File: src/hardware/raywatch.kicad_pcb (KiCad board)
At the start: 2 copper layers, 388 parts, among them J1 Conn_01x02_Pin, J10 Conn_01x04_Pin, J11 Conn_01x04_Pin, J12 Conn_01x02_Pin, J13 Conn_01x02_Pin, J14 Conn_02x08_Top_Bottom, J15 Conn_02x08_Top_Bottom, J16 Conn_02x08_Top_Bottom, J17 Conn_02x08_Top_Bottom, J18 Conn_01x02_Pin, J19 Conn_01x02_Pin, J2 Conn_01x02_Pin, J20 Conn_01x02_Pin, J21 Conn_02x08_Top_Bottom, J22 Conn_01x02_Pin, J23 Conn_01x04_Pin, J24 Conn_01x02_Pin, J25 Conn_01x02_Pin, J26 Conn_01x02_Pin, J27 Conn_01x01_Pin, J28 Conn_01x01_Pin, J29 Conn_01x02_Pin, J3 Conn_01x02_Pin, J30 Conn_01x04_Pin, J31 Conn_01x04_Pin, J32 Conn_01x01_Pin, J33 Conn_01x01_Pin, J34 046809612110846+, J35 Conn_01x02_Pin, J36 Conn_01x02_Pin, J37 Conn_01x02_Pin, J38 Conn_01x02_Pin, J39 Conn_01x02_Pin, J4 Conn_01x02_Pin, J40 Conn_01x02_Pin, J41 Conn_01x02_Pin, J42 Conn_01x02_Pin, J43 Conn_01x02_Pin, J44 Conn_01x02_Pin, J45 Conn_01x02_Pin, J46 Conn_01x02_Pin, J47 Conn_01x02_Pin, J48 Conn_01x02_Pin, J49 Conn_01x02_Pin, J5 Conn_01x02_Pin, J50 Conn_01x04_Pin, J51 MSD-1-A, J52 Conn_01x02_Pin, J53 Conn_01x02_Pin, J54 Conn_01x01_Pin, J55 Conn_01x02_Pin, J56 Conn_01x02_Pin, J57 Conn_01x02_Pin, J58 Conn_01x02_Pin, J59 Conn_01x02_Pin, J6 Conn_01x04_Pin, J60 Conn_01x02_Pin, J61 Conn_01x02_Pin, J62 Conn_01x01_Pin, J63 Conn_01x02_Pin, J64 Conn_01x02_Pin, J65 Conn_01x04_Pin, J66 Conn_01x04_Pin, J67 Conn_01x02_Pin, J68 Conn_01x02_Pin, J69 Conn_01x02_Pin, J7 Conn_01x04_Pin, J70 Conn_02x08_Top_Bottom, J71 Conn_01x02_Pin, J72 Conn_01x01_Pin, J73 Conn_02x08_Top_Bottom, J74 Conn_01x02_Pin, J75 Conn_02x08_Top_Bottom, J76 BM29B0.6-2DS/2-0.35V51, J77 Conn_01x02_Pin, J78 Conn_01x02_Pin, J79 Conn_01x02_Pin, J8 Conn_01x04_Pin, J80 Conn_01x02_Pin, J81 Conn_01x04_Pin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

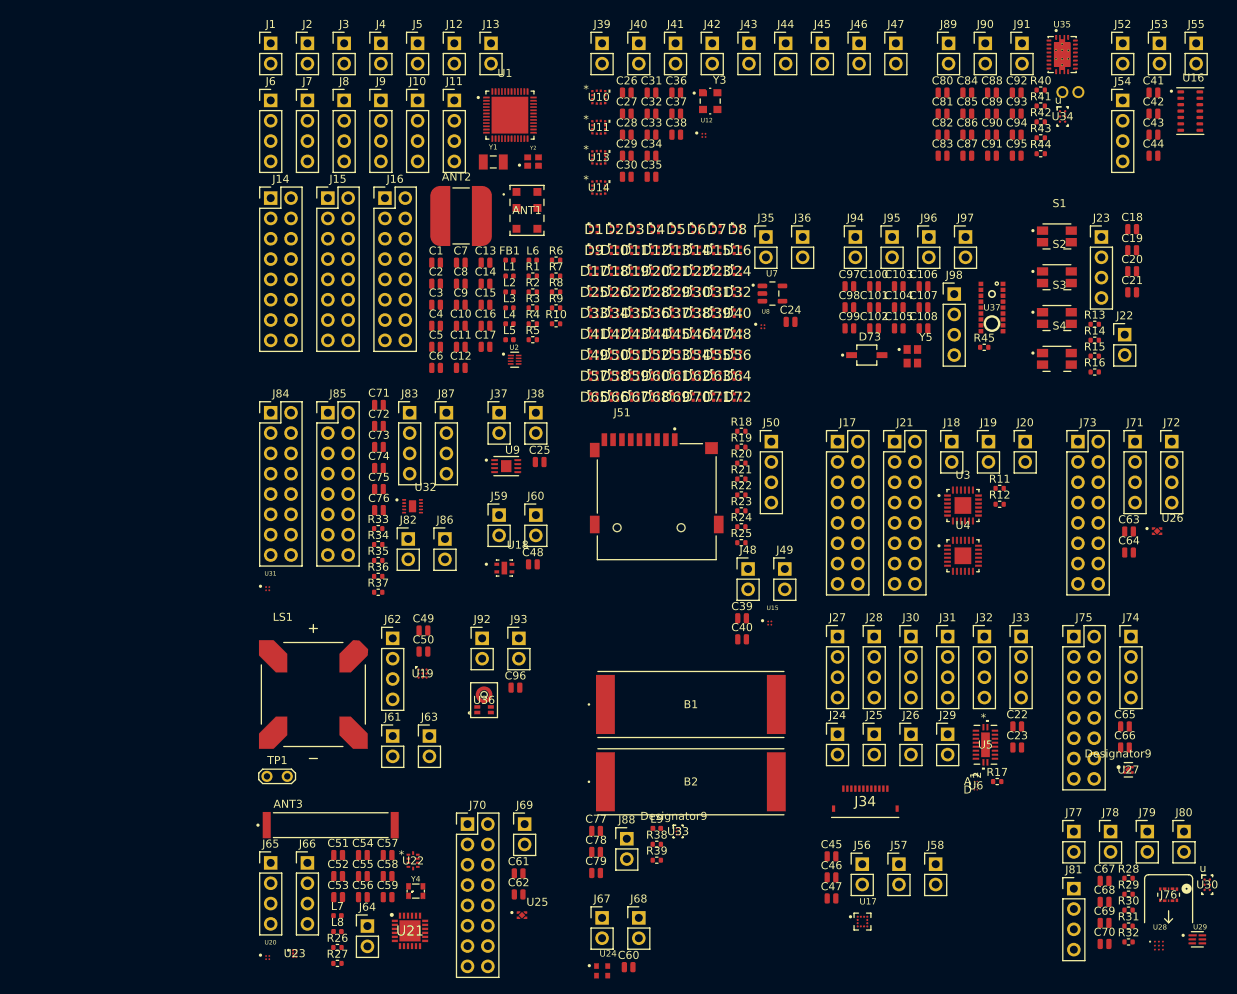
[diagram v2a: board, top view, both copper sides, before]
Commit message: Fixed connector footprints; Changed conectors from 2.54 to 1.27
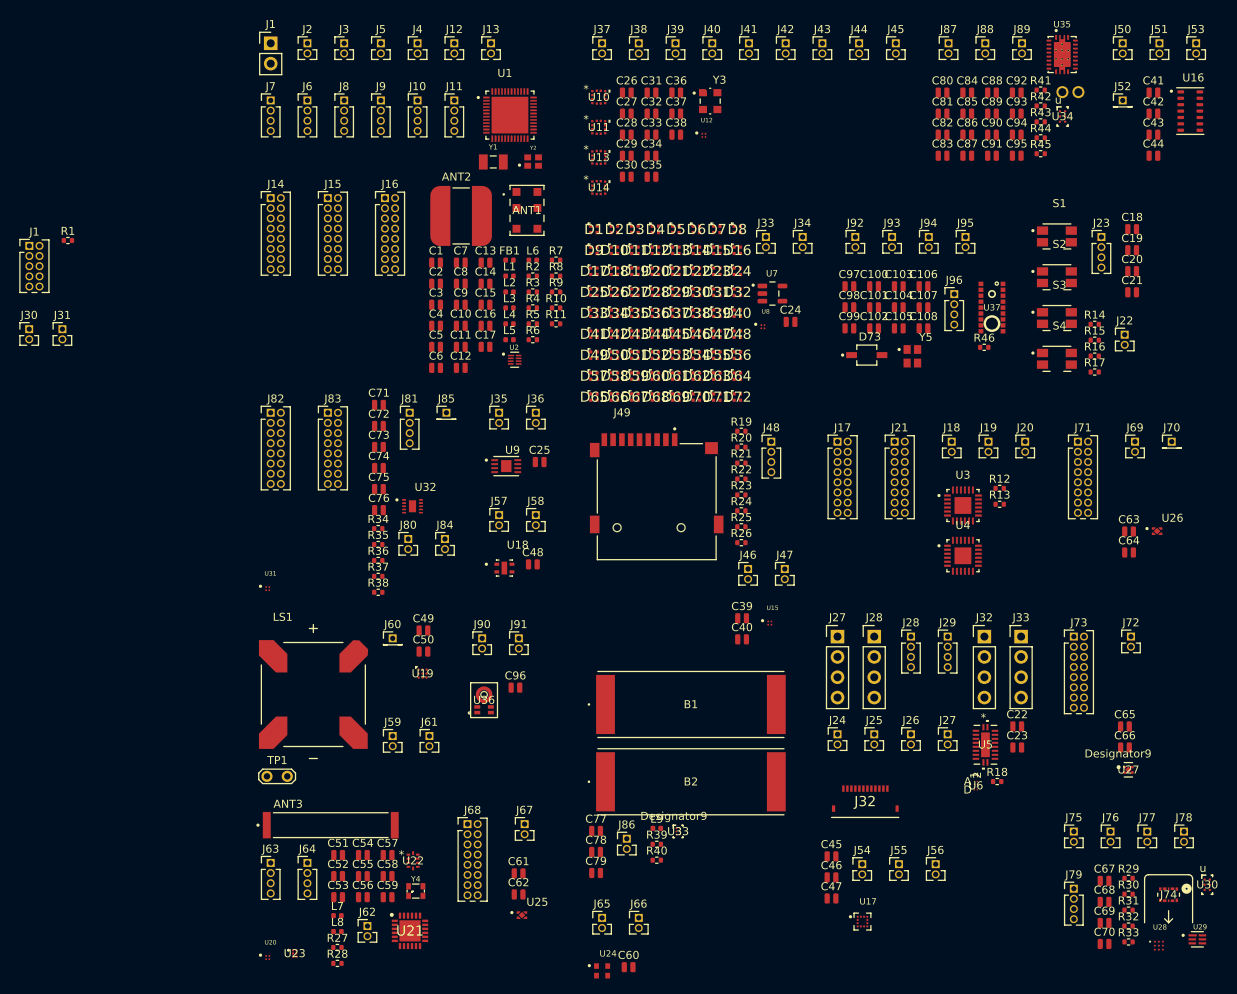
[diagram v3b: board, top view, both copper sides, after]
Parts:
- added J1: Conn_02x05_Odd_Even, Connector_PinHeader_1.27mm:PinHeader_2x05_P1.27mm_Vertical, F.Cu at (54.4, 65.3)
- added J30: Conn_01x02_Pin, Connector_PinHeader_1.27mm:PinHeader_1x02_P1.27mm_Vertical, F.Cu at (54.4, 75.7)
- added J31: Conn_01x02_Pin, Connector_PinHeader_1.27mm:PinHeader_1x02_P1.27mm_Vertical, F.Cu at (58.5, 75.7)
- added R1: 1kΩ, Resistor_SMD:R_0402_1005Metric, F.Cu at (59.2, 64.7)
- J10, J11, J23, J8, J9: footprint Connector_PinHeader_2.54mm:PinHeader_1x04_P2.54mm_Vertical -> Connector_PinHeader_1.27mm:PinHeader_1x04_P1.27mm_Vertical
- J12, J13, J18, J19, J2, J20, J22, J24, J25, J26, J3: footprint Connector_PinHeader_2.54mm:PinHeader_1x02_P2.54mm_Vertical -> Connector_PinHeader_1.27mm:PinHeader_1x02_P1.27mm_Vertical
- J14, J15, J16, J17, J21: footprint Connector_PinHeader_2.54mm:PinHeader_2x08_P2.54mm_Vertical -> Connector_PinHeader_1.27mm:PinHeader_2x08_P1.27mm_Vertical
- J27: renamed from J29; footprint Connector_PinHeader_2.54mm:PinHeader_1x02_P2.54mm_Vertical -> Connector_PinHeader_1.27mm:PinHeader_1x02_P1.27mm_Vertical
- J28: renamed from J30; footprint Connector_PinHeader_2.54mm:PinHeader_1x04_P2.54mm_Vertical -> Connector_PinHeader_1.27mm:PinHeader_1x04_P1.27mm_Vertical
- J29: renamed from J31; footprint Connector_PinHeader_2.54mm:PinHeader_1x04_P2.54mm_Vertical -> Connector_PinHeader_1.27mm:PinHeader_1x04_P1.27mm_Vertical
- J33: renamed from J35; footprint Connector_PinHeader_2.54mm:PinHeader_1x02_P2.54mm_Vertical -> Connector_PinHeader_1.27mm:PinHeader_1x02_P1.27mm_Vertical
- J34: renamed from J36; footprint Connector_PinHeader_2.54mm:PinHeader_1x02_P2.54mm_Vertical -> Connector_PinHeader_1.27mm:PinHeader_1x02_P1.27mm_Vertical
- J35: renamed from J37; footprint Connector_PinHeader_2.54mm:PinHeader_1x02_P2.54mm_Vertical -> Connector_PinHeader_1.27mm:PinHeader_1x02_P1.27mm_Vertical
- J36: renamed from J38; footprint Connector_PinHeader_2.54mm:PinHeader_1x02_P2.54mm_Vertical -> Connector_PinHeader_1.27mm:PinHeader_1x02_P1.27mm_Vertical
- J37: renamed from J39; footprint Connector_PinHeader_2.54mm:PinHeader_1x02_P2.54mm_Vertical -> Connector_PinHeader_1.27mm:PinHeader_1x02_P1.27mm_Vertical
- J38: renamed from J40; footprint Connector_PinHeader_2.54mm:PinHeader_1x02_P2.54mm_Vertical -> Connector_PinHeader_1.27mm:PinHeader_1x02_P1.27mm_Vertical
- J39: renamed from J41; footprint Connector_PinHeader_2.54mm:PinHeader_1x02_P2.54mm_Vertical -> Connector_PinHeader_1.27mm:PinHeader_1x02_P1.27mm_Vertical
- J4: renamed from J5; footprint Connector_PinHeader_2.54mm:PinHeader_1x02_P2.54mm_Vertical -> Connector_PinHeader_1.27mm:PinHeader_1x02_P1.27mm_Vertical
- J40: renamed from J42; footprint Connector_PinHeader_2.54mm:PinHeader_1x02_P2.54mm_Vertical -> Connector_PinHeader_1.27mm:PinHeader_1x02_P1.27mm_Vertical
- J41: renamed from J43; footprint Connector_PinHeader_2.54mm:PinHeader_1x02_P2.54mm_Vertical -> Connector_PinHeader_1.27mm:PinHeader_1x02_P1.27mm_Vertical
- J42: renamed from J44; footprint Connector_PinHeader_2.54mm:PinHeader_1x02_P2.54mm_Vertical -> Connector_PinHeader_1.27mm:PinHeader_1x02_P1.27mm_Vertical
- J43: renamed from J45; footprint Connector_PinHeader_2.54mm:PinHeader_1x02_P2.54mm_Vertical -> Connector_PinHeader_1.27mm:PinHeader_1x02_P1.27mm_Vertical
- J44: renamed from J46; footprint Connector_PinHeader_2.54mm:PinHeader_1x02_P2.54mm_Vertical -> Connector_PinHeader_1.27mm:PinHeader_1x02_P1.27mm_Vertical
- J45: renamed from J47; footprint Connector_PinHeader_2.54mm:PinHeader_1x02_P2.54mm_Vertical -> Connector_PinHeader_1.27mm:PinHeader_1x02_P1.27mm_Vertical
- J46: renamed from J48; footprint Connector_PinHeader_2.54mm:PinHeader_1x02_P2.54mm_Vertical -> Connector_PinHeader_1.27mm:PinHeader_1x02_P1.27mm_Vertical
- J47: renamed from J49; footprint Connector_PinHeader_2.54mm:PinHeader_1x02_P2.54mm_Vertical -> Connector_PinHeader_1.27mm:PinHeader_1x02_P1.27mm_Vertical
- J48: renamed from J50; footprint Connector_PinHeader_2.54mm:PinHeader_1x04_P2.54mm_Vertical -> Connector_PinHeader_1.27mm:PinHeader_1x04_P1.27mm_Vertical
- J5: renamed from J4; footprint Connector_PinHeader_2.54mm:PinHeader_1x02_P2.54mm_Vertical -> Connector_PinHeader_1.27mm:PinHeader_1x02_P1.27mm_Vertical
- J50: renamed from J52; footprint Connector_PinHeader_2.54mm:PinHeader_1x02_P2.54mm_Vertical -> Connector_PinHeader_1.27mm:PinHeader_1x02_P1.27mm_Vertical
- J51: renamed from J53; footprint Connector_PinHeader_2.54mm:PinHeader_1x02_P2.54mm_Vertical -> Connector_PinHeader_1.27mm:PinHeader_1x02_P1.27mm_Vertical
- J52: renamed from J54; footprint Connector_PinHeader_2.54mm:PinHeader_1x04_P2.54mm_Vertical -> Connector_PinHeader_1.27mm:PinHeader_1x01_P1.27mm_Vertical
- J53: renamed from J55; footprint Connector_PinHeader_2.54mm:PinHeader_1x02_P2.54mm_Vertical -> Connector_PinHeader_1.27mm:PinHeader_1x02_P1.27mm_Vertical
- J54: renamed from J56; footprint Connector_PinHeader_2.54mm:PinHeader_1x02_P2.54mm_Vertical -> Connector_PinHeader_1.27mm:PinHeader_1x02_P1.27mm_Vertical
- J55: renamed from J57; footprint Connector_PinHeader_2.54mm:PinHeader_1x02_P2.54mm_Vertical -> Connector_PinHeader_1.27mm:PinHeader_1x02_P1.27mm_Vertical
- J56: renamed from J58; footprint Connector_PinHeader_2.54mm:PinHeader_1x02_P2.54mm_Vertical -> Connector_PinHeader_1.27mm:PinHeader_1x02_P1.27mm_Vertical
- J57: renamed from J59; footprint Connector_PinHeader_2.54mm:PinHeader_1x02_P2.54mm_Vertical -> Connector_PinHeader_1.27mm:PinHeader_1x02_P1.27mm_Vertical
- J58: renamed from J60; footprint Connector_PinHeader_2.54mm:PinHeader_1x02_P2.54mm_Vertical -> Connector_PinHeader_1.27mm:PinHeader_1x02_P1.27mm_Vertical
- J59: renamed from J61; footprint Connector_PinHeader_2.54mm:PinHeader_1x02_P2.54mm_Vertical -> Connector_PinHeader_1.27mm:PinHeader_1x02_P1.27mm_Vertical
- J6: renamed from J7; footprint Connector_PinHeader_2.54mm:PinHeader_1x04_P2.54mm_Vertical -> Connector_PinHeader_1.27mm:PinHeader_1x04_P1.27mm_Vertical
- J60: renamed from J62; footprint Connector_PinHeader_2.54mm:PinHeader_1x04_P2.54mm_Vertical -> Connector_PinHeader_1.27mm:PinHeader_1x01_P1.27mm_Vertical
- J61: renamed from J63; footprint Connector_PinHeader_2.54mm:PinHeader_1x02_P2.54mm_Vertical -> Connector_PinHeader_1.27mm:PinHeader_1x02_P1.27mm_Vertical
- J62: renamed from J64; footprint Connector_PinHeader_2.54mm:PinHeader_1x02_P2.54mm_Vertical -> Connector_PinHeader_1.27mm:PinHeader_1x02_P1.27mm_Vertical
- J63: renamed from J65; footprint Connector_PinHeader_2.54mm:PinHeader_1x04_P2.54mm_Vertical -> Connector_PinHeader_1.27mm:PinHeader_1x04_P1.27mm_Vertical
- J64: renamed from J66; footprint Connector_PinHeader_2.54mm:PinHeader_1x04_P2.54mm_Vertical -> Connector_PinHeader_1.27mm:PinHeader_1x04_P1.27mm_Vertical
- J65: renamed from J67; footprint Connector_PinHeader_2.54mm:PinHeader_1x02_P2.54mm_Vertical -> Connector_PinHeader_1.27mm:PinHeader_1x02_P1.27mm_Vertical
- J66: renamed from J68; footprint Connector_PinHeader_2.54mm:PinHeader_1x02_P2.54mm_Vertical -> Connector_PinHeader_1.27mm:PinHeader_1x02_P1.27mm_Vertical
- J67: renamed from J69; footprint Connector_PinHeader_2.54mm:PinHeader_1x02_P2.54mm_Vertical -> Connector_PinHeader_1.27mm:PinHeader_1x02_P1.27mm_Vertical
- J68: renamed from J70; footprint Connector_PinHeader_2.54mm:PinHeader_2x08_P2.54mm_Vertical -> Connector_PinHeader_1.27mm:PinHeader_2x08_P1.27mm_Vertical
- J69: renamed from J71; footprint Connector_PinHeader_2.54mm:PinHeader_1x04_P2.54mm_Vertical -> Connector_PinHeader_1.27mm:PinHeader_1x02_P1.27mm_Vertical
- J7: renamed from J6; footprint Connector_PinHeader_2.54mm:PinHeader_1x04_P2.54mm_Vertical -> Connector_PinHeader_1.27mm:PinHeader_1x04_P1.27mm_Vertical
- J70: renamed from J72; footprint Connector_PinHeader_2.54mm:PinHeader_1x04_P2.54mm_Vertical -> Connector_PinHeader_1.27mm:PinHeader_1x01_P1.27mm_Vertical
- J71: renamed from J73; footprint Connector_PinHeader_2.54mm:PinHeader_2x08_P2.54mm_Vertical -> Connector_PinHeader_1.27mm:PinHeader_2x08_P1.27mm_Vertical
- J72: renamed from J74; footprint Connector_PinHeader_2.54mm:PinHeader_1x04_P2.54mm_Vertical -> Connector_PinHeader_1.27mm:PinHeader_1x02_P1.27mm_Vertical
- J73: renamed from J75; footprint Connector_PinHeader_2.54mm:PinHeader_2x08_P2.54mm_Vertical -> Connector_PinHeader_1.27mm:PinHeader_2x08_P1.27mm_Vertical
- J75: renamed from J77; footprint Connector_PinHeader_2.54mm:PinHeader_1x02_P2.54mm_Vertical -> Connector_PinHeader_1.27mm:PinHeader_1x02_P1.27mm_Vertical
- J76: renamed from J78; footprint Connector_PinHeader_2.54mm:PinHeader_1x02_P2.54mm_Vertical -> Connector_PinHeader_1.27mm:PinHeader_1x02_P1.27mm_Vertical
- J77: renamed from J79; footprint Connector_PinHeader_2.54mm:PinHeader_1x02_P2.54mm_Vertical -> Connector_PinHeader_1.27mm:PinHeader_1x02_P1.27mm_Vertical
- J78: renamed from J80; footprint Connector_PinHeader_2.54mm:PinHeader_1x02_P2.54mm_Vertical -> Connector_PinHeader_1.27mm:PinHeader_1x02_P1.27mm_Vertical
- J79: renamed from J81; footprint Connector_PinHeader_2.54mm:PinHeader_1x04_P2.54mm_Vertical -> Connector_PinHeader_1.27mm:PinHeader_1x04_P1.27mm_Vertical
- J80: renamed from J82; footprint Connector_PinHeader_2.54mm:PinHeader_1x02_P2.54mm_Vertical -> Connector_PinHeader_1.27mm:PinHeader_1x02_P1.27mm_Vertical
- J81: renamed from J83; footprint Connector_PinHeader_2.54mm:PinHeader_1x04_P2.54mm_Vertical -> Connector_PinHeader_1.27mm:PinHeader_1x04_P1.27mm_Vertical
- J82: renamed from J84; footprint Connector_PinHeader_2.54mm:PinHeader_2x08_P2.54mm_Vertical -> Connector_PinHeader_1.27mm:PinHeader_2x08_P1.27mm_Vertical
- J83: renamed from J85; footprint Connector_PinHeader_2.54mm:PinHeader_2x08_P2.54mm_Vertical -> Connector_PinHeader_1.27mm:PinHeader_2x08_P1.27mm_Vertical
- J84: renamed from J86; footprint Connector_PinHeader_2.54mm:PinHeader_1x02_P2.54mm_Vertical -> Connector_PinHeader_1.27mm:PinHeader_1x02_P1.27mm_Vertical
- J85: renamed from J87; footprint Connector_PinHeader_2.54mm:PinHeader_1x04_P2.54mm_Vertical -> Connector_PinHeader_1.27mm:PinHeader_1x01_P1.27mm_Vertical
- J86: renamed from J88; footprint Connector_PinHeader_2.54mm:PinHeader_1x02_P2.54mm_Vertical -> Connector_PinHeader_1.27mm:PinHeader_1x02_P1.27mm_Vertical
- J87: renamed from J89; footprint Connector_PinHeader_2.54mm:PinHeader_1x02_P2.54mm_Vertical -> Connector_PinHeader_1.27mm:PinHeader_1x02_P1.27mm_Vertical
- J88: renamed from J90; footprint Connector_PinHeader_2.54mm:PinHeader_1x02_P2.54mm_Vertical -> Connector_PinHeader_1.27mm:PinHeader_1x02_P1.27mm_Vertical
- J89: renamed from J91; footprint Connector_PinHeader_2.54mm:PinHeader_1x02_P2.54mm_Vertical -> Connector_PinHeader_1.27mm:PinHeader_1x02_P1.27mm_Vertical
- J90: renamed from J92; footprint Connector_PinHeader_2.54mm:PinHeader_1x02_P2.54mm_Vertical -> Connector_PinHeader_1.27mm:PinHeader_1x02_P1.27mm_Vertical
- J91: renamed from J93; footprint Connector_PinHeader_2.54mm:PinHeader_1x02_P2.54mm_Vertical -> Connector_PinHeader_1.27mm:PinHeader_1x02_P1.27mm_Vertical
- J92: renamed from J94; footprint Connector_PinHeader_2.54mm:PinHeader_1x02_P2.54mm_Vertical -> Connector_PinHeader_1.27mm:PinHeader_1x02_P1.27mm_Vertical
- J93: renamed from J95; footprint Connector_PinHeader_2.54mm:PinHeader_1x02_P2.54mm_Vertical -> Connector_PinHeader_1.27mm:PinHeader_1x02_P1.27mm_Vertical
- J94: renamed from J96; footprint Connector_PinHeader_2.54mm:PinHeader_1x02_P2.54mm_Vertical -> Connector_PinHeader_1.27mm:PinHeader_1x02_P1.27mm_Vertical
- J95: renamed from J97; footprint Connector_PinHeader_2.54mm:PinHeader_1x02_P2.54mm_Vertical -> Connector_PinHeader_1.27mm:PinHeader_1x02_P1.27mm_Vertical
- J96: renamed from J98; footprint Connector_PinHeader_2.54mm:PinHeader_1x04_P2.54mm_Vertical -> Connector_PinHeader_1.27mm:PinHeader_1x04_P1.27mm_Vertical
- renumbered J34 to J32, J51 to J49, J76 to J74, R9 to R10, R10 to R11, R11 to R12, R12 to R13, R13 to R14, R14 to R15, R15 to R16, R16 to R17, R17 to R18, R18 to R19, R1 to R2, R19 to R20, R20 to R21, R21 to R22, R22 to R23, R23 to R24, R24 to R25, R25 to R26, R26 to R27, R27 to R28, R28 to R29, R2 to R3, R29 to R30, R30 to R31, R31 to R32, R32 to R33, R33 to R34, R34 to R35, R35 to R36, R36 to R37, R37 to R38, R38 to R39, R3 to R4, R39 to R40, R40 to R41, R41 to R42, R42 to R43, R43 to R44, R44 to R45, R45 to R46, R4 to R5, R5 to R6, R6 to R7, R7 to R8, R8 to R9
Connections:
- net Net-(J10-Pin_2) renamed /MC: Microcontroller/P2.07
- U1 pad 26: Net-(J1-Pin_1) -> Net-(J1-Pin_4)
- U5 pad 12: Net-(J32-Pin_1) -> Net-(J30-Pin_2)
- U5 pad 13: /Display/HRINT -> Net-(J30-Pin_1)
- U5 pad 8: /Display/HRINT1V8 -> Net-(J31-Pin_1)
- U5 pad 9: Net-(J33-Pin_1) -> Net-(J31-Pin_2)

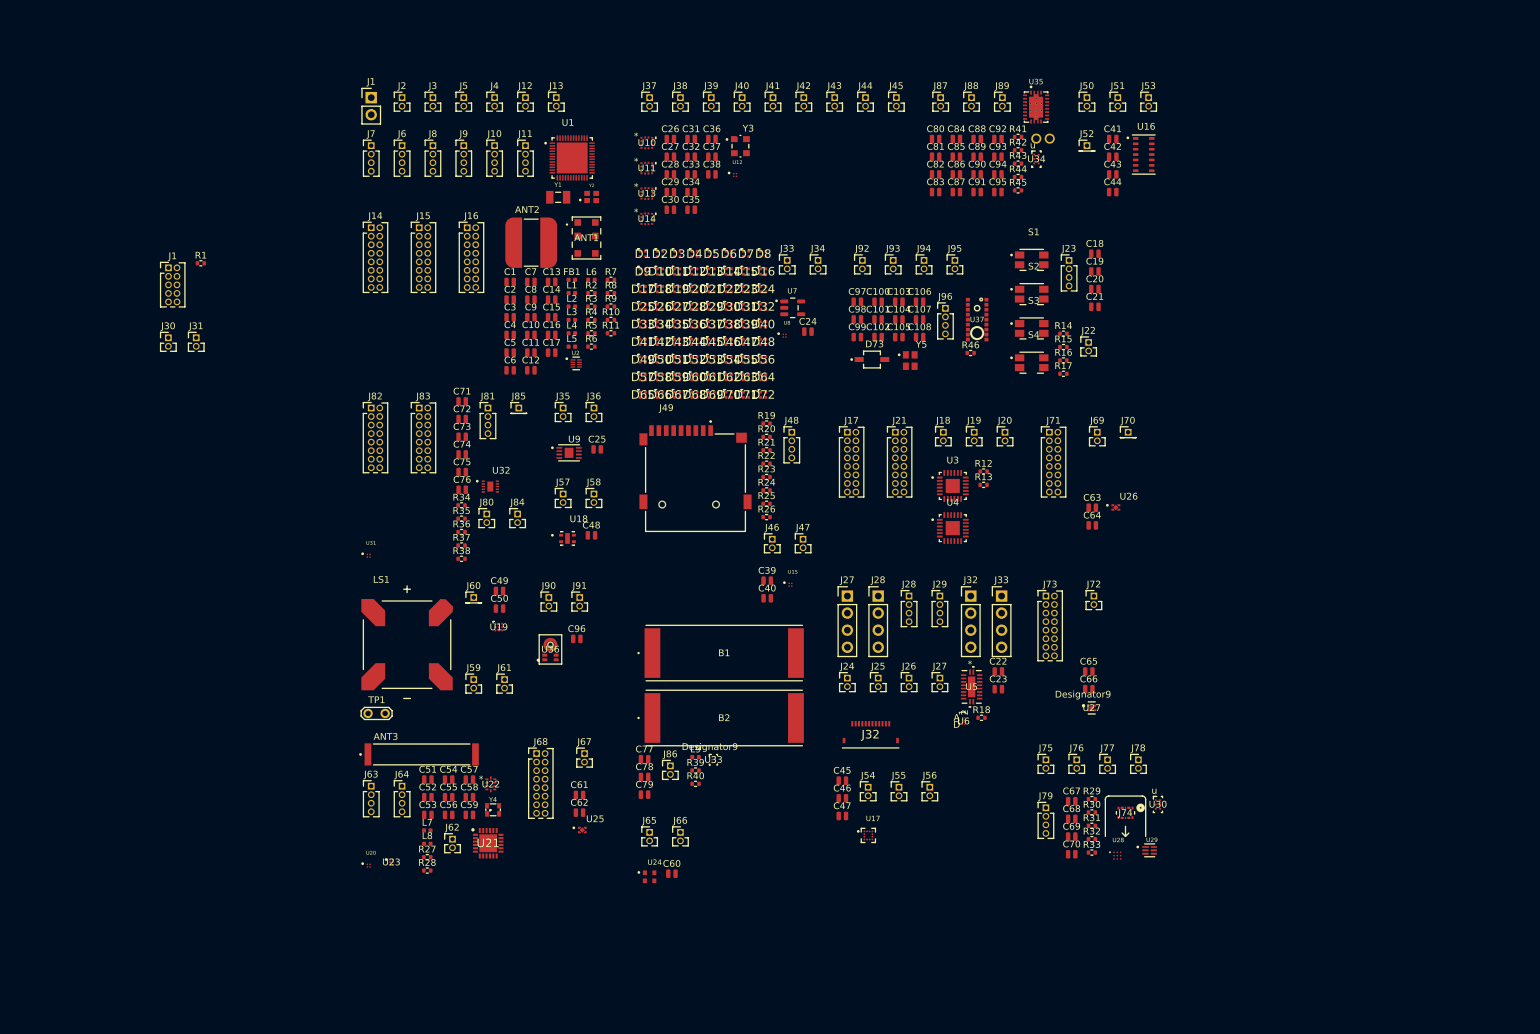
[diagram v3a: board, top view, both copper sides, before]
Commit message: Sorted footprints into modules
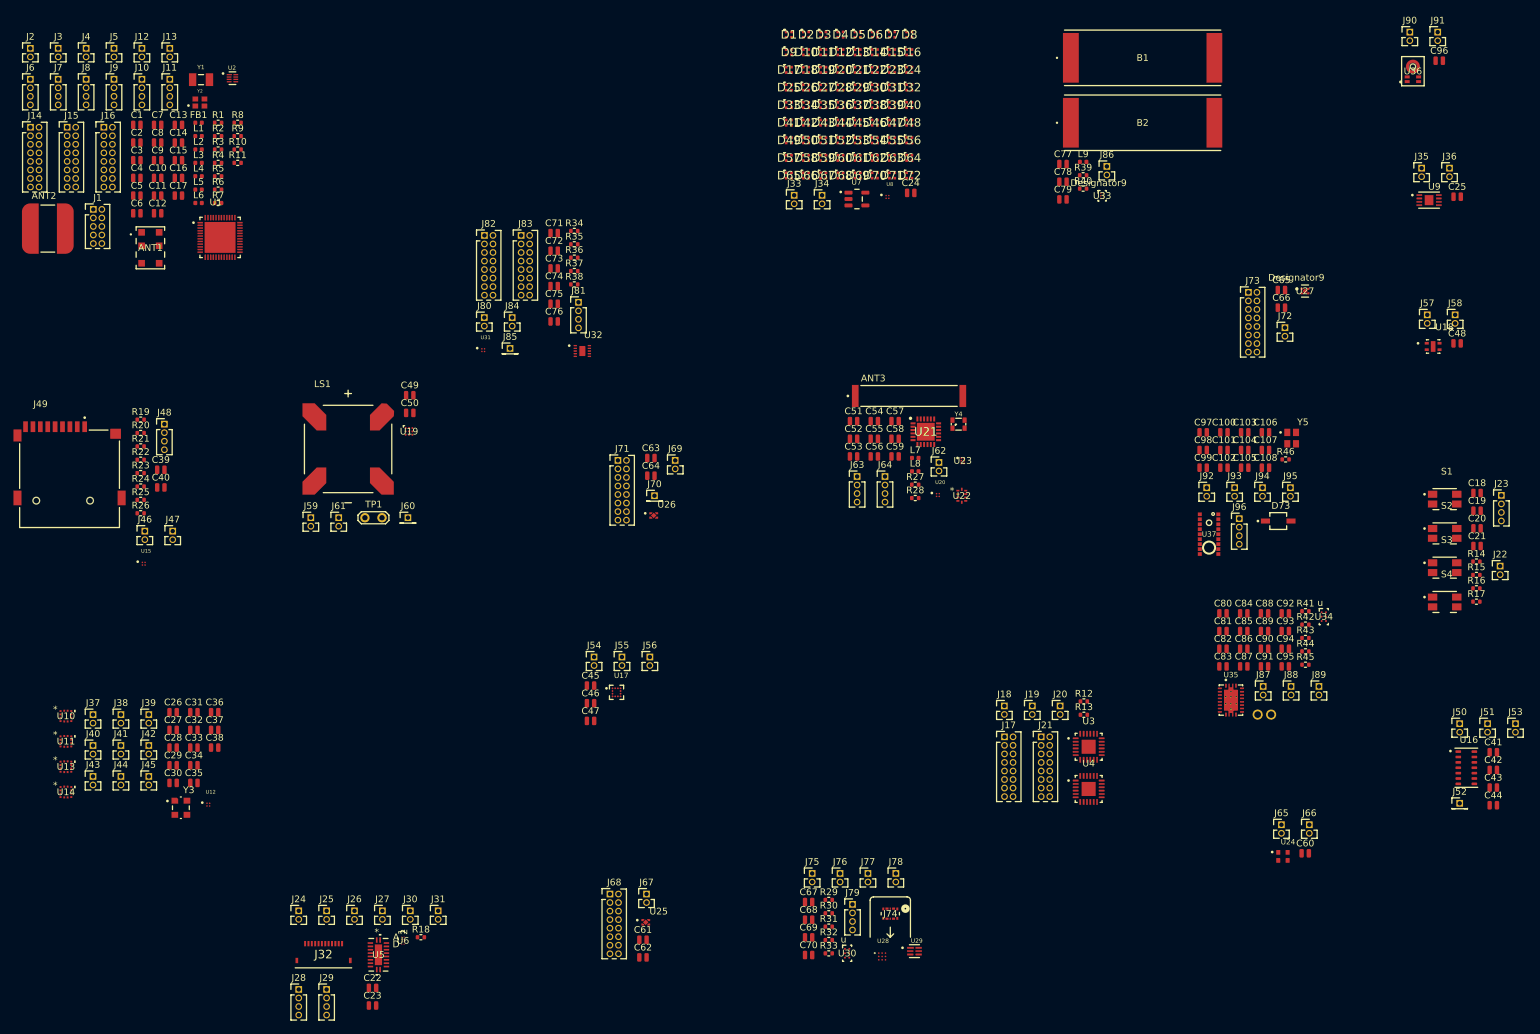
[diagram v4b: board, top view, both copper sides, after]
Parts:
- removed the J1 at (84.5, 40.0)
- removed the J1 at (54.4, 65.3)
- removed the J27 at (155.4, 114.2)
- removed the J27 at (169.2, 126.4)
- removed the J28 at (160.0, 114.2)
- removed the J28 at (164.6, 114.2)
- removed the J32 at (158.8, 135.0)
- removed the J32 at (173.8, 114.2)
- removed the J33 at (178.3, 114.2)
- removed the J33 at (146.4, 64.2)
- added J1: Conn_02x05_Odd_Even, Connector_PinHeader_1.27mm:PinHeader_2x05_P1.27mm_Vertical, F.Cu at (43.2, 56.6)
- added J27: Conn_01x02_Pin, Connector_PinHeader_1.27mm:PinHeader_1x02_P1.27mm_Vertical, F.Cu at (86.2, 161.0)
- added J28: Conn_01x04_Pin, Connector_PinHeader_1.27mm:PinHeader_1x04_P1.27mm_Vertical, F.Cu at (73.8, 172.7)
- added J32: 046809612110846+, Project:046809612110846, F.Cu at (77.4, 167.7)
- added J33: Conn_01x02_Pin, Connector_PinHeader_1.27mm:PinHeader_1x02_P1.27mm_Vertical, F.Cu at (147.5, 54.5)
- moved C96 154.5 mm to (243.5, 34.5)
- moved U36 154.5 mm to (239.5, 36.1)
- moved J90 153.3 mm to (239.1, 30.2)
- moved J91 152.9 mm to (243.2, 30.2)
- moved J45 150.3 mm to (51.4, 141.0)
- moved J44 149.9 mm to (47.3, 141.0)
- moved J43 149.6 mm to (43.1, 141.0)
- moved J42 137.1 mm to (51.4, 136.4)
- moved J41 136.8 mm to (47.3, 136.4)
- moved J40 136.5 mm to (43.1, 136.4)
- moved C25 133.4 mm to (246.1, 54.7)
- moved U9 133.4 mm to (241.9, 55.2)
- moved J35 132.6 mm to (240.8, 50.5)
- moved J36 132.2 mm to (245.0, 50.5)
- moved C48 131.9 mm to (246.1, 76.6)
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
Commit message: Created Microphone PCB
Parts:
- moved U36 14.9 mm to (251.6, 27.5)
- moved C96 8.90 mm to (249.0, 27.5), turned to 90 degrees
- moved J91 8.24 mm to (251.0, 33.0), turned to 90 degrees
- moved J90 8.17 mm to (246.8, 33.0), turned to -90 degrees
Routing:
- net +3V3: track 0.00 -> 7.73 mm
- net /Microphone/PDMCLK: track 0.00 -> 4.10 mm
- net /Microphone/PDMDATA: track 0.00 -> 4.08 mm
- net GND: track 0.00 -> 0.64 mm
- added copper zone on B.Cu, net GND
- added copper zone on F.Cu, net GND
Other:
- board outline added: 13 x 13.5 mm
- board text added: "3.3V"
- board text added: "CL"
- board text added: "DA"
- board text added: "GND"

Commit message: Fixes; Added TPM PCB
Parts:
- C1, C10, C100, C101, C102, C103, C104, C105, C106, C107, C108, C11, C12, C13, C14, C15, C16, C17, C18, C19, C2, C20, C21, C22, C23, C24, C25, C26, C27, C28, C29, C3, C30, C31, C32, C33, C34, C35, C36, C37, C38, C39, C4, C40, C41, C42, C43, C44, C45, C46, C47, C48, C49, C5, C50, C51, C52, C53, C54, C55, C56, C57, C58, C59, C6, C60, C61, C62, C63, C64, C65, C66, C67, C68, C69, C7, C70, C71, C72, C73, C74, C75, C76, C77, C78, C79, C8, C80, C81, C82, C83, C84, C85, C86, C87, C88, C89, C9, C90, C91, C92, C93, C94, C95, C96, C97, C98, C99: footprint Capacitor_SMD:C_0504_1310Metric -> Capacitor_SMD:C_0402_1005Metric
- moved J35 17.6 mm to (256.2, 59.0), turned to 90 degrees
- moved U9 13.6 mm to (255.2, 52.3), turned to -90 degrees
- moved J36 12.1 mm to (253.5, 59.0), turned to -90 degrees
- moved C25 10.4 mm to (256.5, 55.2)
- moved C96 0.06 mm to (249.0, 27.6)
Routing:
- net /TPM/SDA: track 0.00 -> 6.18 mm
- net /TPM/SCL: track 0.00 -> 6.13 mm
- net +3V3: track 7.73 -> 13.1 mm
- net GND: track 0.64 -> 0.00 mm
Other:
- board size 13 x 13.5 mm -> 17.1 x 39.2 mm
- board text added: "3V3"
- board text removed: "3.3V"
- board text removed: "GND"
